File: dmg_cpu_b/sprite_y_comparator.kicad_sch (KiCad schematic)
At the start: 116 parts

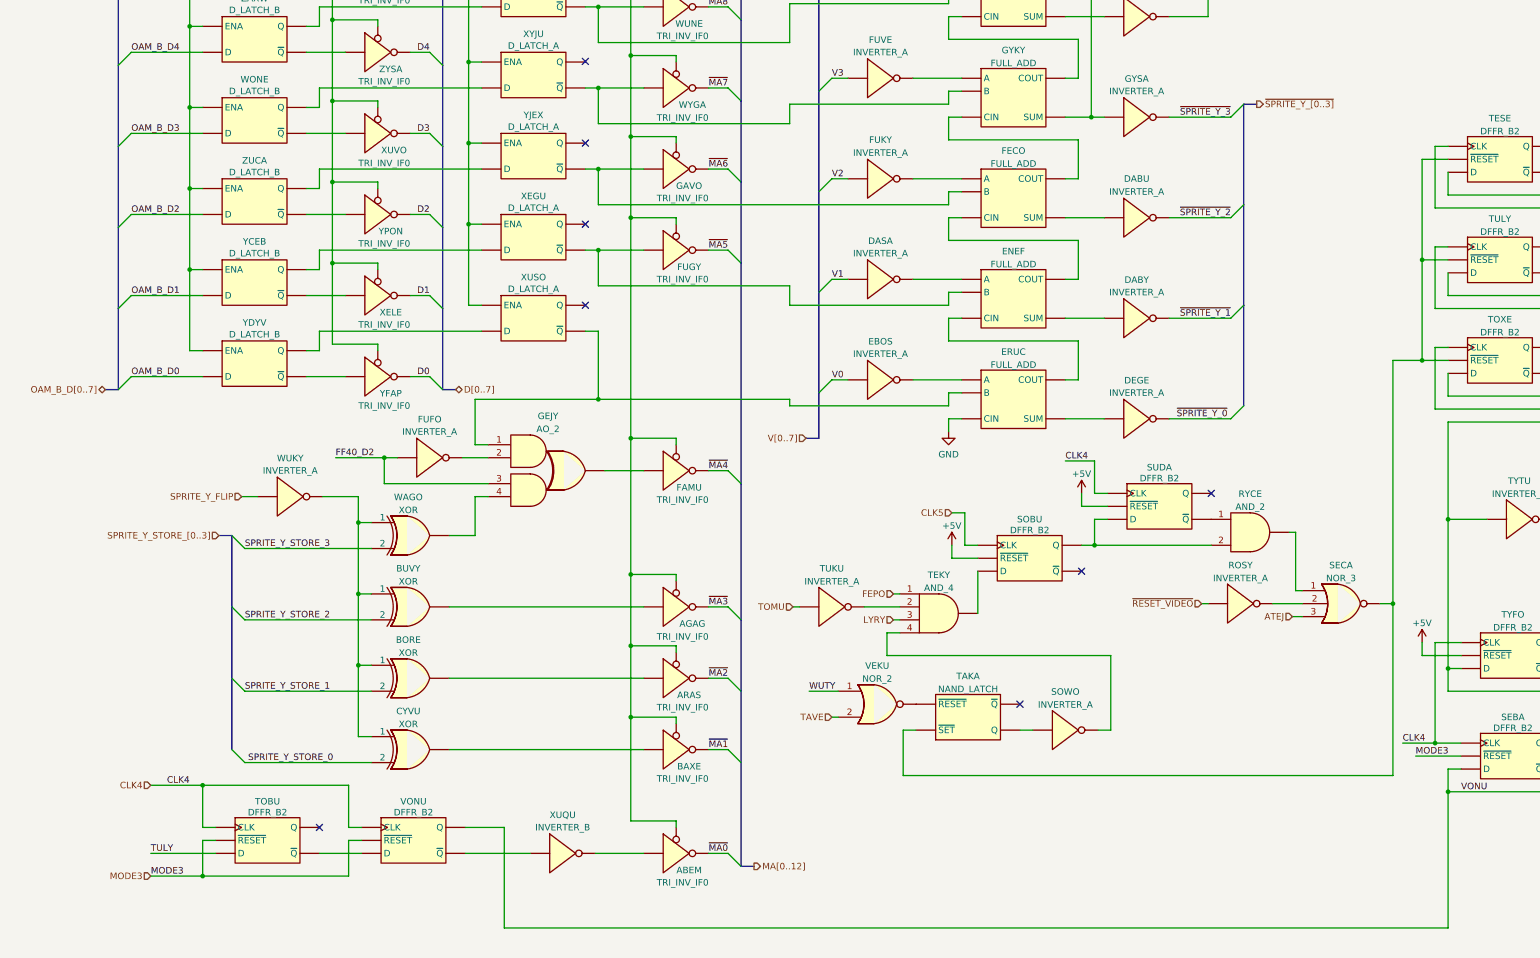
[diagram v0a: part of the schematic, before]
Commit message: more oam sheets added. Some are still work in progress.
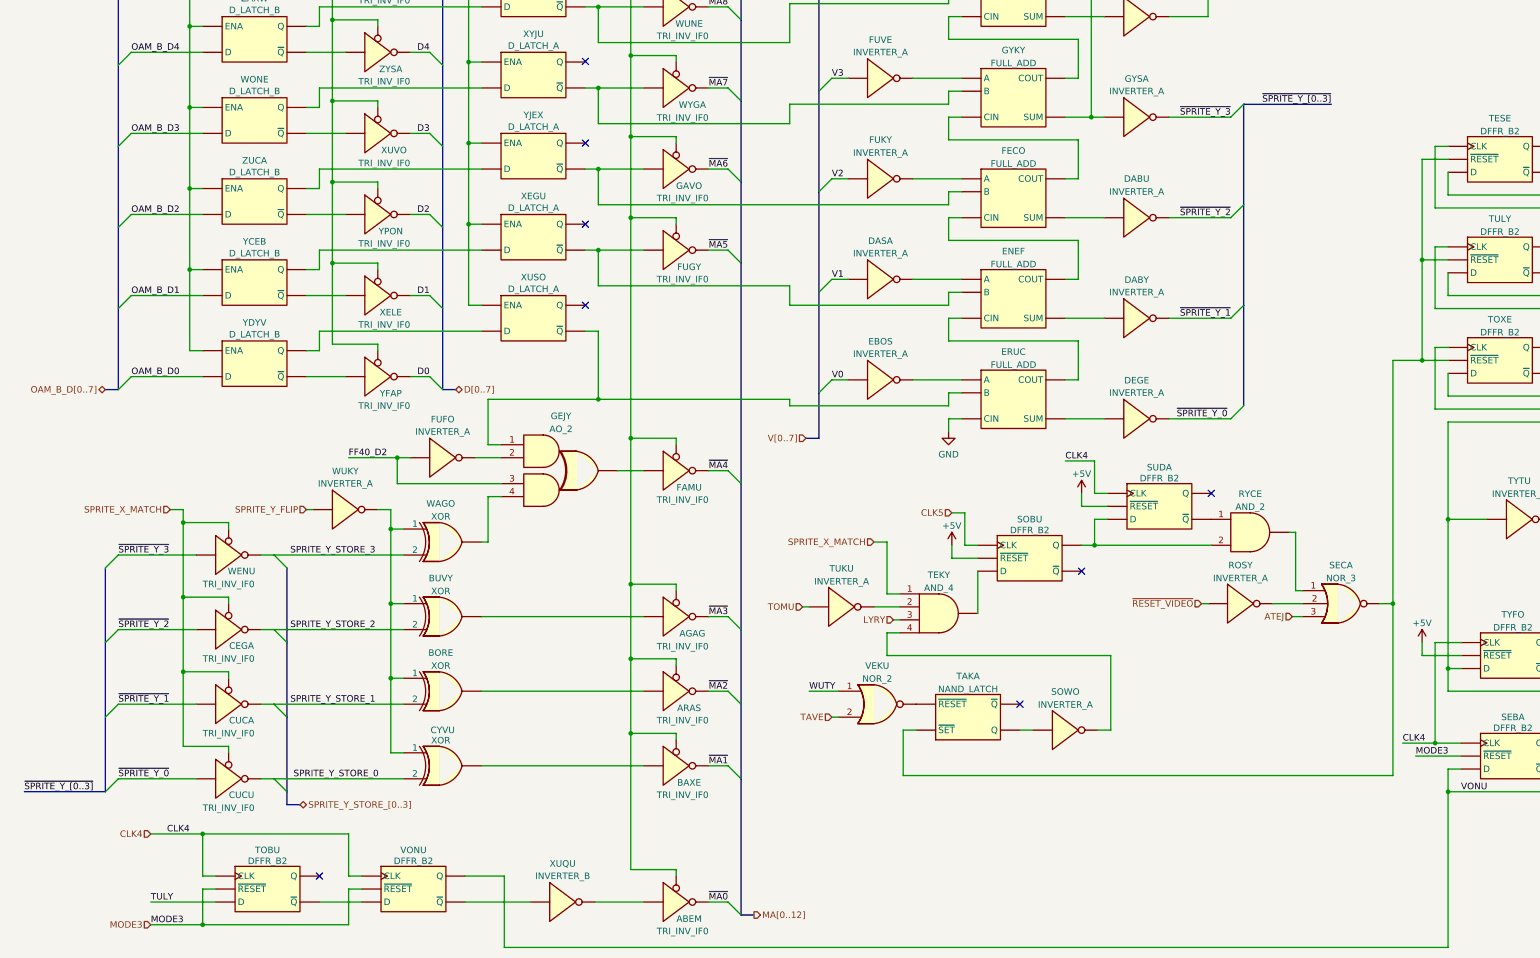
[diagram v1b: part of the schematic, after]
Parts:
- added CEGA, CUCA, CUCU, WENU: TRI_INV_IF0, symbol DMG_CPU_Cells:TRI_INV_IF0
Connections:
- net SPRITE_Y_STORE_0: now also CUCU.3
- net SPRITE_Y_STORE_1: now also CUCA.3
- net SPRITE_Y_STORE_2: now also CEGA.3
- net SPRITE_Y_STORE_3: now also WENU.3
- net ~{SPRITE_Y_0}: now also CUCU.2
- net ~{SPRITE_Y_1}: now also CUCA.2
- net ~{SPRITE_Y_2}: now also CEGA.2
- net ~{SPRITE_Y_3}: now also WENU.2
- net FEPO renamed SPRITE_X_MATCH
- net SPRITE_X_MATCH: now also CEGA.1 (~{ENA}), CUCA.1 (~{ENA}), CUCU.1 (~{ENA}), WENU.1 (~{ENA})
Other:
- moved on the sheet: ABEM, AGAG, ARAS, BAXE, BORE, BUVY, CYVU, FUFO, GEJY, TOBU, TUKU, VONU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

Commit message: More OAM sheets added.
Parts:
- removed XEFY: INVERTER_A, symbol DMG_CPU_Cells:INVERTER_A
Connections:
- net CLK3 renamed ~{OAM_CLK}
- net ~{OAM_B_CPU_RD} renamed ~{OAM_B_RD}
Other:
- note added: "OAM B D[0..7] gives the sprite Y position during parsing and will determine if the sprite appears on the current line. If it does, D[0..3] gets stored to define the offset in the sprite char. During rendering, it will contain the Tile address which be used to fecth sprite char data in VRAM."
- moved on the sheet: ABEM, ABON, AGAG, ARAS, BAXE, BORE, BUVY, CEGA, CUCA, CUCU, CYVU, DABU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

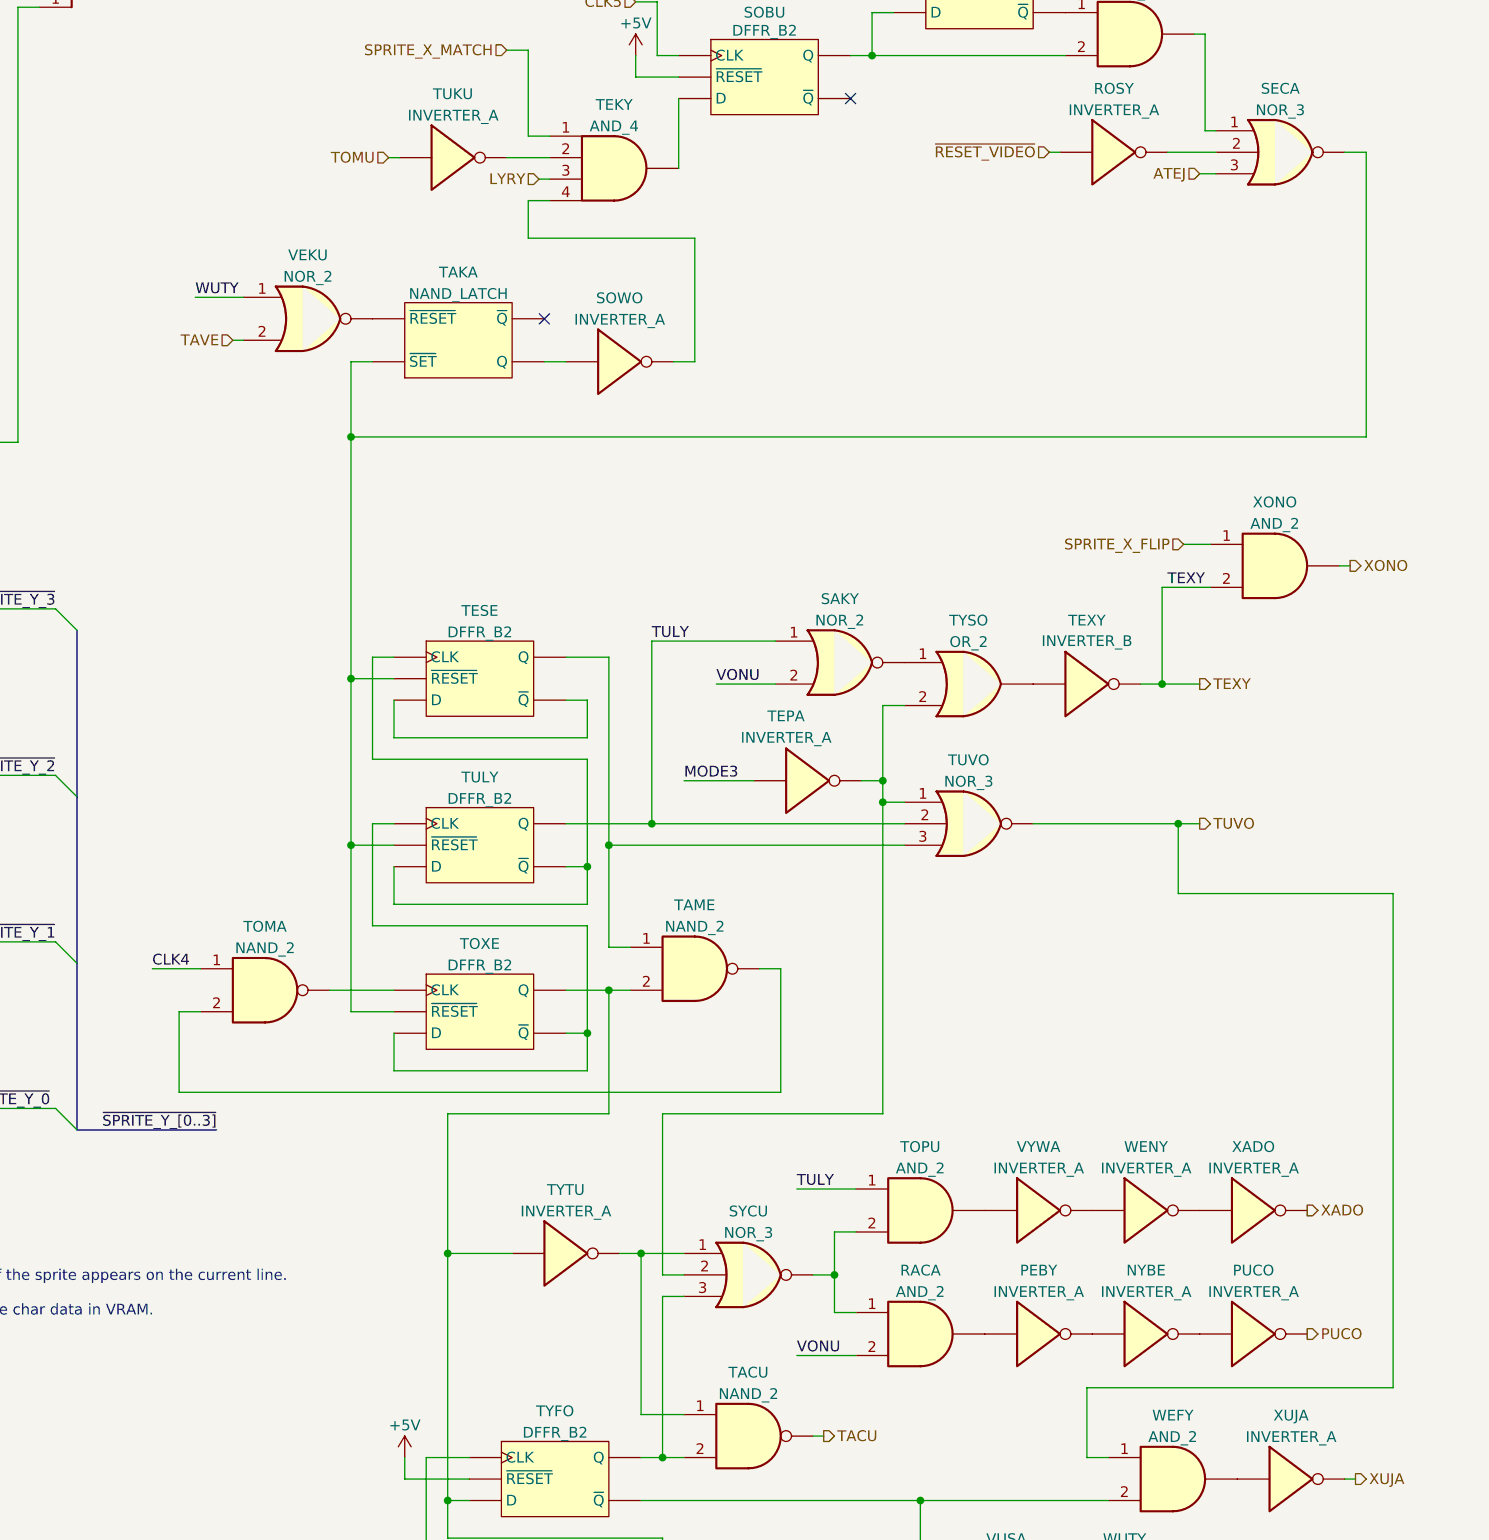
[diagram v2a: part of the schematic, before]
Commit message: bg and sp px shifters added.
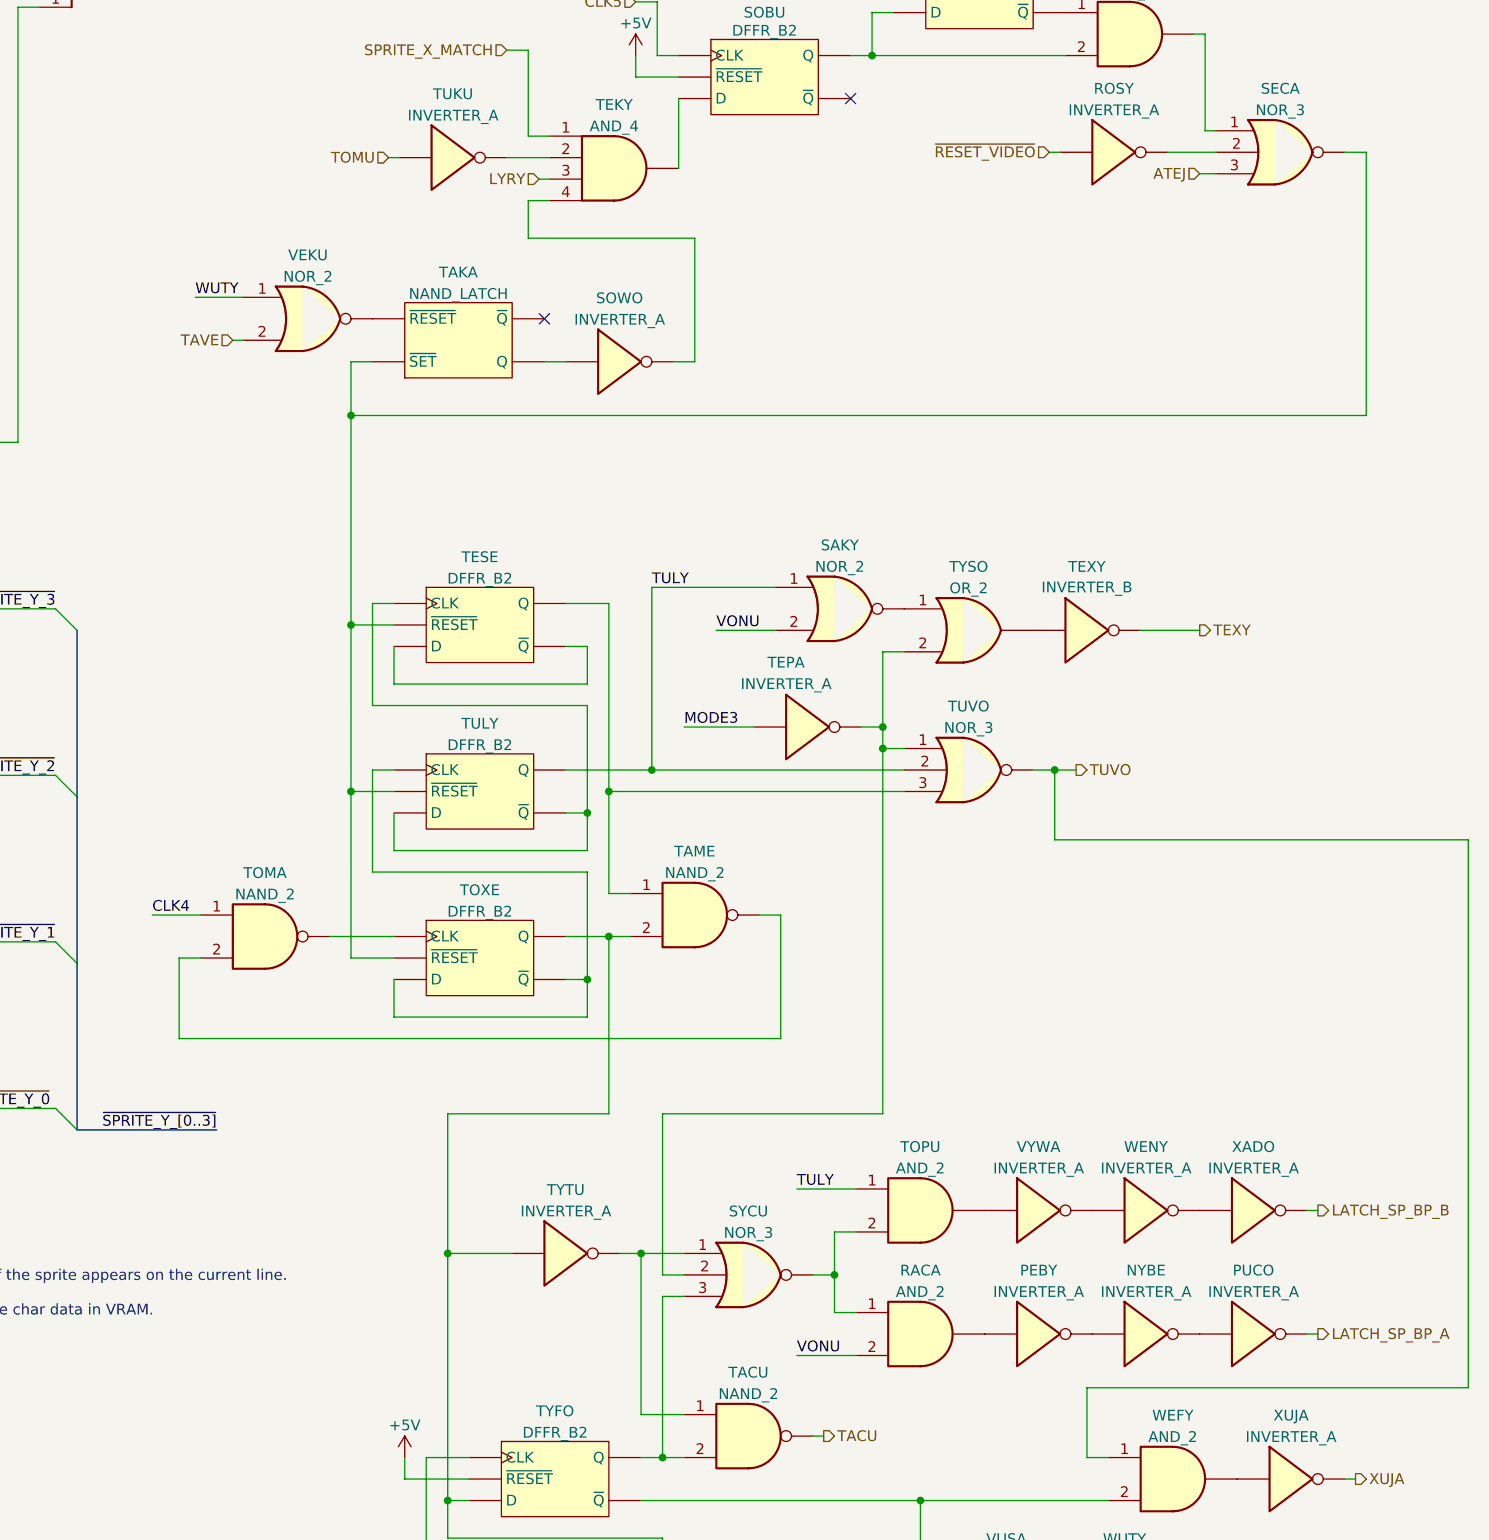
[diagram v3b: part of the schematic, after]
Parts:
- removed XONO: AND_2, symbol DMG_CPU_Cells:AND_2
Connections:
- net PUCO renamed LATCH_SP_BP_A
- net XADO renamed LATCH_SP_BP_B
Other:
- moved on the sheet: SAKY, TAME, TEPA, TESE, TEXY, TOMA, TOXE, TULY, TUVO, TYSO

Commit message: All sheets captured. Serious tidying is required in PPU section.
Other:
- company: (none) -> CC-BY-SA-4.0 Régis Galland & Michael Singer -- Derived work from Furrtek
- title: (none) -> DMG CPU B
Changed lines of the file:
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@@
 (kicad_sch (version 20211123) (generator eeschema)
   (paper "A3")
+  (title_block
+    (title "DMG CPU B")
+    (date "2022-05-19")
+    (rev "0")
+    (company "CC-BY-SA-4.0 Régis Galland & Michael Singer -- Derived work from Furrtek")
+    (comment 1 "https://github.com/msinger/dmg-schematics")
+  )
   (junction (at 74.295 84.455) (diameter 0) (color 0 0 0 0)
   )

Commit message: Fixes based on review. + various other edits.
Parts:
- added TAVA: INVERTER_A, symbol DMG_CPU_Cells:INVERTER_A
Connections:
- net CLK4: now also TAVA.1
- net CLK5: no longer names the net of SOBU.1 (CLK)
- net CLK5: now also TAVA.2
- net TEXY renamed SP_BP_CYS
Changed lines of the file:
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@@
     (stroke (width 0) (type default) (color 0 0 0 0))
   )
+  (wire (pts (xy 307.34 40.005) (xy 309.88 40.005))
+    (stroke (width 0) (type default) (color 0 0 0 0))
+  )
   (wire (pts (xy 213.995 178.435) (xy 206.375 178.435))
     (stroke (width 0) (type default) (color 0 0 0 0))
@@
     (stroke (width 0) (type default) (color 0 0 0 0))
   )
+  (wire (pts (xy 288.925 40.005) (xy 294.64 40.005))
+    (stroke (width 0) (type default) (color 0 0 0 0))
+  )
   (wire (pts (xy 74.295 100.33) (xy 74.295 116.205))
     (stroke (width 0) (type default) (color 0 0 0 0))
@@
     (stroke (width 0) (type default) (color 0 0 0 0))
   )
-  (wire (pts (xy 309.88 47.625) (xy 309.88 53.975))
-    (stroke (width 0) (type default) (color 0 0 0 0))
-  )
   (wire (pts (xy 301.625 130.81) (xy 276.225 130.81))
     (stroke (width 0) (type default) (color 0 0 0 0))
@@
     (stroke (width 0) (type default) (color 0 0 0 0))
   )
-  (wire (pts (xy 105.41 25.4) (xy 110.49 25.4))
+  (wire (pts (xy 98.425 25.4) (xy 110.49 25.4))
     (stroke (width 0) (type default) (color 0 0 0 0))
   )
@@
     (stroke (width 0) (type default) (color 0 0 0 0))
   )
-  (wire (pts (xy 307.34 47.625) (xy 309.88 47.625))
-    (stroke (width 0) (type default) (color 0 0 0 0))
-  )
   (wire (pts (xy 126.365 104.775) (xy 162.56 104.775))
     (stroke (width 0) (type default) (color 0 0 0 0))
@@
     (stroke (width 0) (type default) (color 0 0 0 0))
   )
+  (wire (pts (xy 309.88 40.005) (xy 309.88 53.975))
+    (stroke (width 0) (type default) (color 0 0 0 0))
+  )
   (bus (pts (xy 154.305 84.455) (xy 154.305 100.33))
     (stroke (width 0) (type default) (color 0 0 0 0))
@@
     (effects (font (size 1.27 1.27)) (justify left bottom))
   )
-  (label "TEXY" (at 105.41 25.4 0)
+  (label "SP_BP_CYS" (at 98.425 25.4 0)
     (effects (font (size 1.27 1.27)) (justify left bottom))
   )
@@
     (effects (font (size 1.27 1.27)) (justify left bottom))
   )
+  (label "CLK4" (at 288.925 40.005 0)
+    (effects (font (size 1.27 1.27)) (justify left bottom))
+  )
   (label "~{SPRITE_Y_[0..3]}" (at 257.81 180.975 180)
     (effects (font (size 1.27 1.27)) (justify right bottom))
@@
     (effects (font (size 1.27 1.27)) (justify right))
   )
-  (hierarchical_label "CLK5" (shape input) (at 307.34 47.625 180)
-    (effects (font (size 1.27 1.27)) (justify right))
-  )
   (hierarchical_label "SPRITE_X_MATCH" (shape input) (at 292.1 53.34 180)
     (effects (font (size 1.27 1.27)) (justify right))
@@
     (effects (font (size 1.27 1.27)) (justify right))
   )
-  (hierarchical_label "TEXY" (shape output) (at 374.015 121.92 0)
+  (hierarchical_label "SP_BP_CYS" (shape output) (at 374.015 121.92 0)
     (effects (font (size 1.27 1.27)) (justify left))
   )
@@
     (pin "3")
   )
+  (symbol (lib_id "DMG_CPU_Cells:INVERTER_A") (at 300.99 40.005 0) (unit 1)
+    (in_bom yes) (on_board yes) (fields_autoplaced)
+    (property "Reference" "TAVA" (id 0) (at 300.99 32.4952 0))
+    (property "Value" "INVERTER_A" (id 1) (at 300.99 35.0321 0))
+    (property "Footprint" "" (id 2) (at 298.45 40.005 0)
+      (effects (font (size 1.27 1.27)) hide)
+    )
+    (property "Datasheet" "http://iceboy.a-singer.de/doc/dmg_cells.html#inv_a" (id 3) (at 302.26 47.625 0)
+      (effects (font (size 1.27 1.27)) hide)
+    )
+    (pin "1")
+    (pin "2")
+  )
   (symbol (lib_id "DMG_CPU_Cells:NOR_2") (at 268.605 85.09 0) (unit 1)
